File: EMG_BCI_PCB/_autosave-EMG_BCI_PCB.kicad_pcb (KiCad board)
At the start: 4 copper layers, 74 parts, among them J1 Conn_01x08_Pin, J2 2.54 mm header, U1 INA350, U2 ADA4807-4ARUZ, U3 ADA4807-4ARUZ, U5 MCP1727-3302xSN, U7 LM2776, U8 MCP1501-18xCH, U9 MCP3202

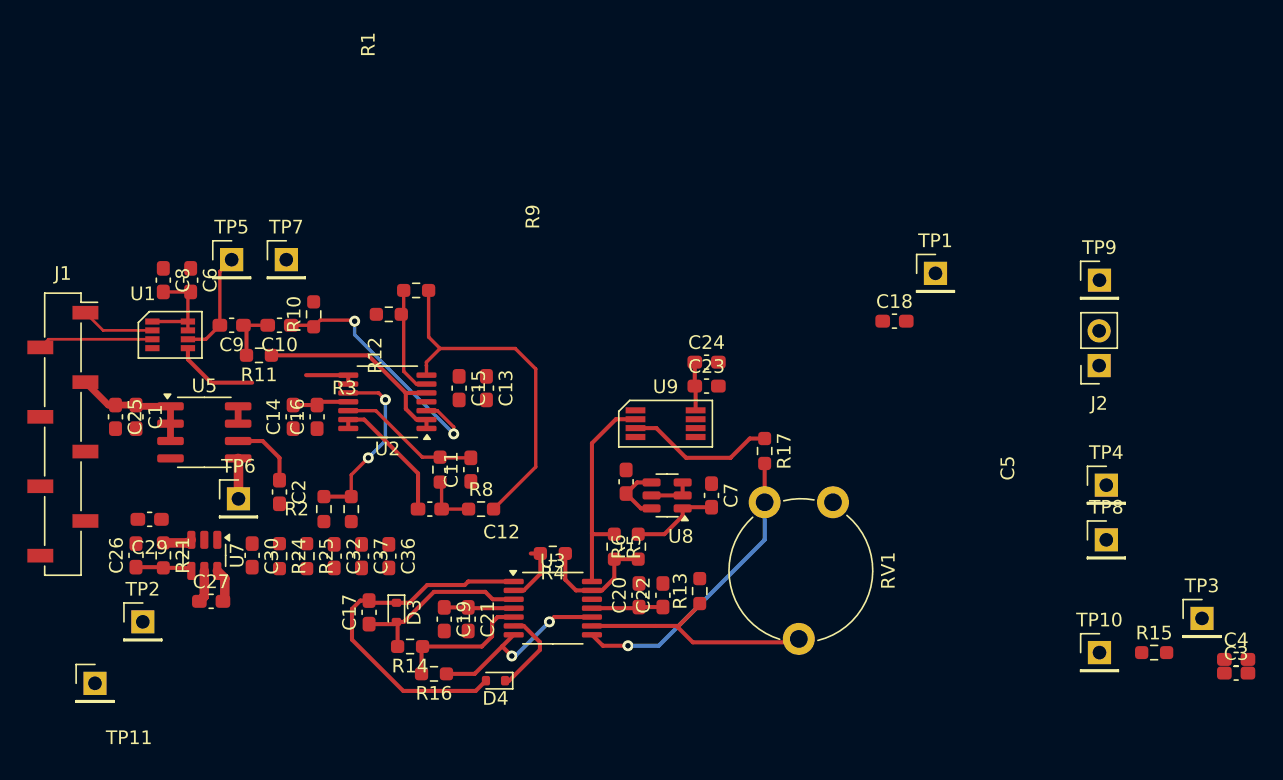
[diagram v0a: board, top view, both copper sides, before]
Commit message: Initial placement and routing
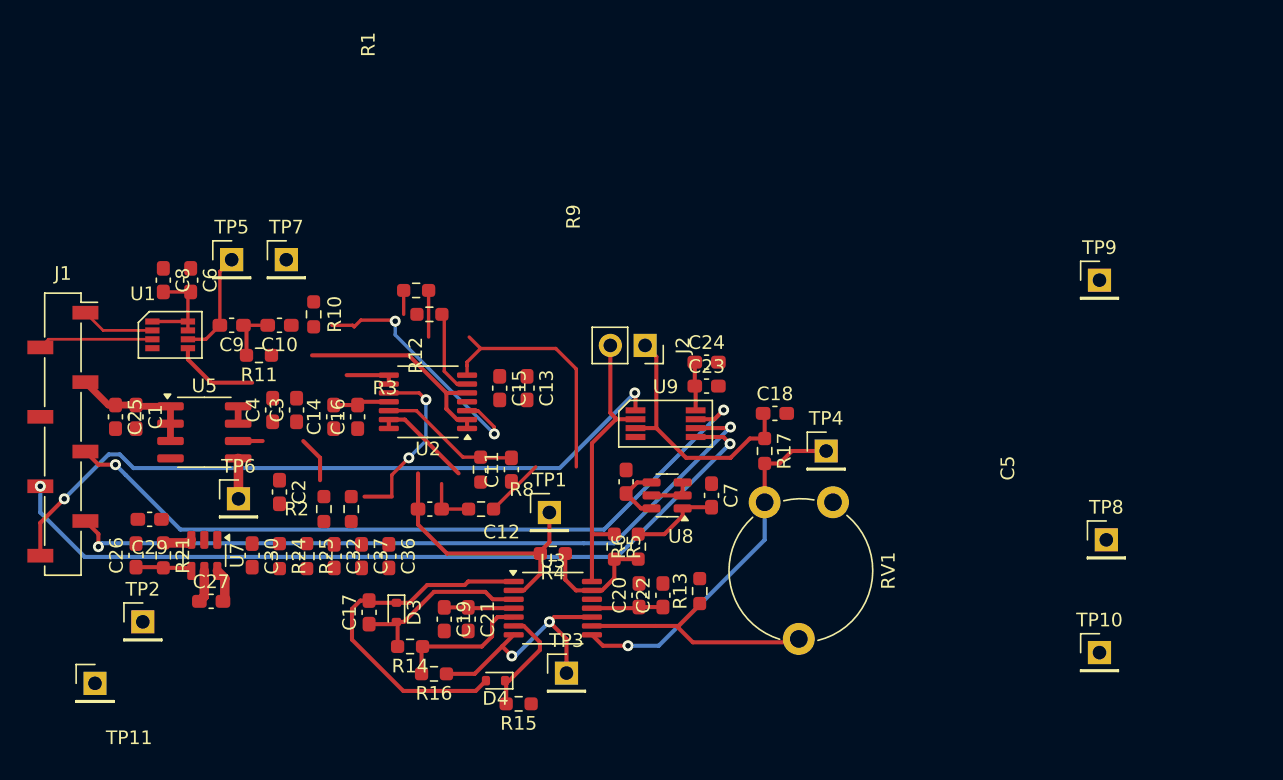
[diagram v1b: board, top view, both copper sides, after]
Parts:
- moved C4 72.8 mm to (115.0, 96.0), turned to 90 degrees
- moved C3 71.4 mm to (116.8, 96.0), turned to 90 degrees
- moved TP3 46.7 mm to (136.5, 115.2)
- moved R15 46.7 mm to (133.0, 117.5), turned to 180 degrees
- moved J2 33.3 mm to (142.2, 91.3), turned to -90 degrees
- moved TP1 33.2 mm to (135.2, 103.5)
- moved TP4 20.7 mm to (155.5, 99.0)
- moved C18 11.1 mm to (151.8, 96.2)
- moved C11 2.97 mm to (132.5, 100.4)
- moved C13 2.97 mm to (133.6, 94.4)
- moved C14 2.97 mm to (119.5, 96.5)
- moved C15 2.97 mm to (131.6, 94.4)
- moved C16 2.97 mm to (121.2, 96.5)
- moved R12 2.97 mm to (126.5, 89.0)
- moved R9 2.97 mm to (130.2, 100.4)
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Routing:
- net /SPI_DIN: track 0.00 -> 59.9 mm, vias 0 -> 2
- net /SPI_CLK: track 0.00 -> 55.0 mm, vias 0 -> 2
- net /SPI_DOUT: track 0.00 -> 54.7 mm, vias 0 -> 2
- net /SPI_CS: track 0.00 -> 52.0 mm, vias 0 -> 2
- net /EMG_FrontEnd/LP_OUT: track 14.6 -> 28.2 mm
- net /EMG_ADC/AdcCh1: track 10.9 -> 19.2 mm
- net /EMG_ADC/AdcCh0: track 15.7 -> 21.3 mm
- net Net-(R17-Pad2): track 21.8 -> 26.6 mm
- net Net-(U3C-+): track 14.1 -> 18.4 mm
- net Net-(D4-K): track 6.47 -> 8.19 mm
